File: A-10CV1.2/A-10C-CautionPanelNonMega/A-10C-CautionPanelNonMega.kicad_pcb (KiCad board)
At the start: 2 copper layers, 129.5 x 85.1 mm, 29 parts, among them J1 Barrel_Jack, J10 Conn_01x24, J11 Conn_01x24, J13 Conn_01x03, J2 Nano Pins 1-15, J3 Nano Pins 16-30 (reversed), J4 Serial Tx/Rx, J8 Conn_01x24, J9 Conn_01x24, Q1 BC338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

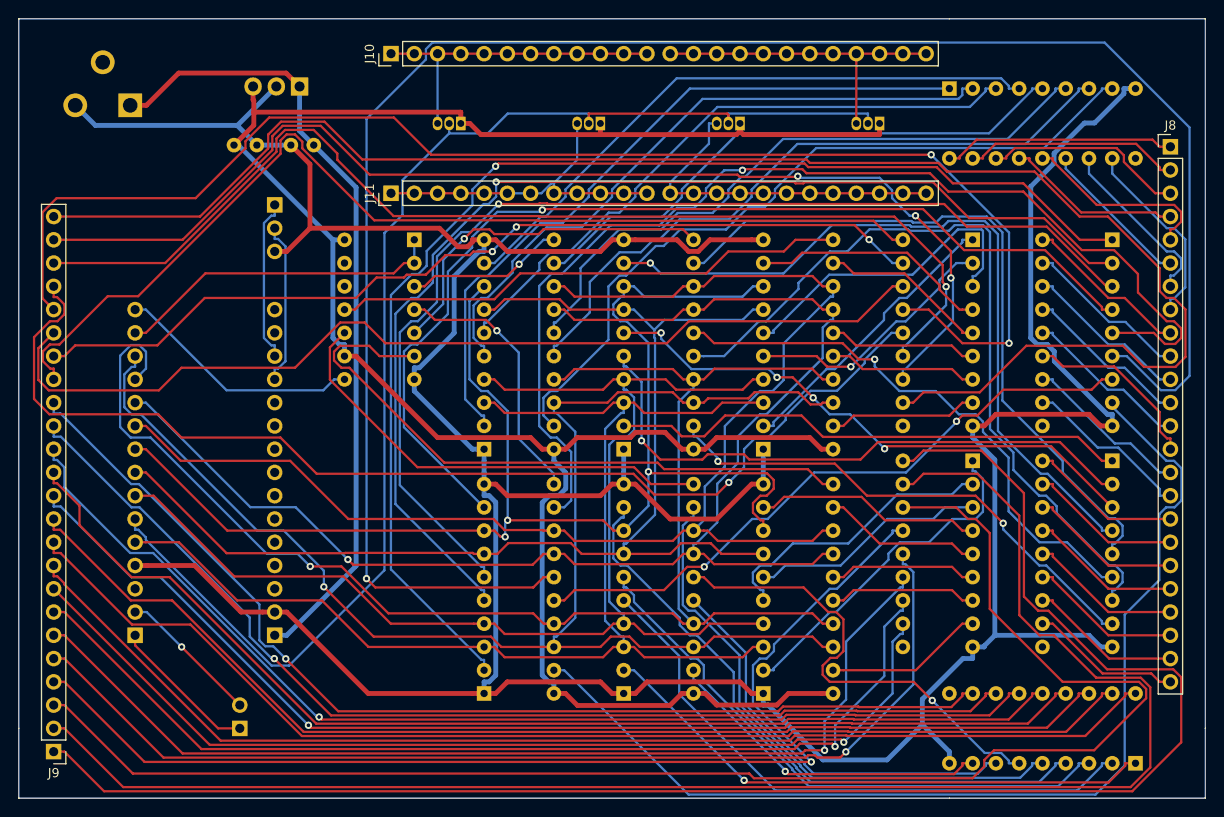
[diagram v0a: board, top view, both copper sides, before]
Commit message: First bits of working code completed. May be changed in favor of single event vs 48 events.
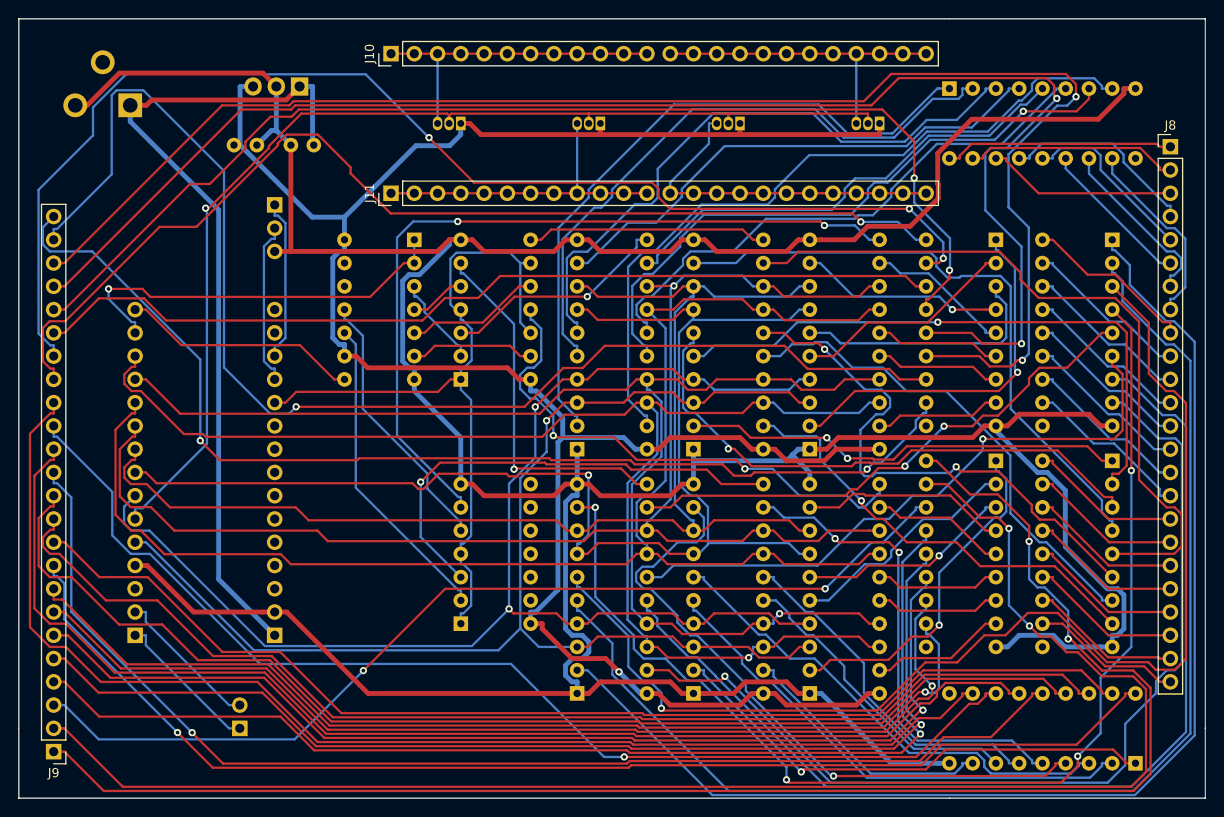
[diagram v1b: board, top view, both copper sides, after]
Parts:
- added U15: 74LS08, Package_DIP:DIP-14_W7.62mm, B.Cu at (97.8, 85.1)
- added U16: 74LS08, Package_DIP:DIP-14_W7.62mm, B.Cu at (97.8, 111.8)
- moved U10 10.2 mm to (110.5, 119.4)
- moved U9 10.2 mm to (110.5, 92.7)
- moved U11 7.62 mm to (123.2, 92.7)
- moved U13 7.62 mm to (123.2, 119.4)
- moved U12 5.08 mm to (135.9, 119.4)
- moved U14 5.08 mm to (135.9, 92.7)
- moved U5 2.54 mm to (156.2, 94.0)
- moved U7 2.54 mm to (156.2, 69.8)
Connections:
- J3 pad 11: Net-(J3-Pad11) -> /CE
- U8 pad 10: /CP4 -> /CPP4
- U8 pad 11: /CP5 -> /CPP5
- U8 pad 3: /CP0 -> /CPP0
- U8 pad 4: /CP1 -> /CPP1
- U8 pad 5: /CP2 -> /CPP2
- U8 pad 6: /CP3 -> /CPP3
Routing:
- net Net-(U10-Pad15): track 207.1 -> 68.0 mm
- net /CE: track 0.00 -> 83.4 mm
- net Net-(U10-Pad12): track 121.1 -> 59.2 mm, vias 1 -> 2
- net /DO3: track 167.3 -> 107.5 mm, vias 0 -> 2
- net /FO8: track 178.7 -> 120.2 mm, vias 0 -> 2
- net /FO6: track 122.7 -> 166.9 mm, vias 1 -> 2
- net Net-(U10-Pad16): track 71.0 -> 114.5 mm, vias 2 -> 0
- net /FO5: track 123.0 -> 164.1 mm, vias 1 -> 2
- net /FO2: track 100.4 -> 136.8 mm
- net /CPP4: track 0.00 -> 34.6 mm
- net Net-(U11-Pad16): track 86.8 -> 54.3 mm
- net /CP5: track 56.5 -> 86.7 mm, vias 0 -> 2
- net /CPP5: track 0.00 -> 29.7 mm
- net GND: track 420.4 -> 448.0 mm
- net /FO4: track 151.8 -> 126.1 mm
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
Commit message: Tweaking timing for Nano to 8 bit interface.
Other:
- board text added: "Rx Tx"
- board text added: "Serial Data (From RS-485)"
- board text removed: "R T"
- board text removed: "Serial Data (RS-485)"
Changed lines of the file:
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@@
     )
   )
-  (gr_text "R\n\nT" (at 76.2 121.92) (layer B.SilkS)
+  (gr_text "Rx\n\nTx" (at 77.47 121.92) (layer B.SilkS)
     (effects (font (size 1 1) (thickness 0.15)) (justify mirror))
   )
-  (gr_text "Serial Data (RS-485)" (at 86.36 120.65) (layer B.SilkS)
+  (gr_text " Serial Data \n(From RS-485)" (at 86.36 121.92) (layer B.SilkS)
     (effects (font (size 1 1) (thickness 0.15)) (justify mirror))
   )

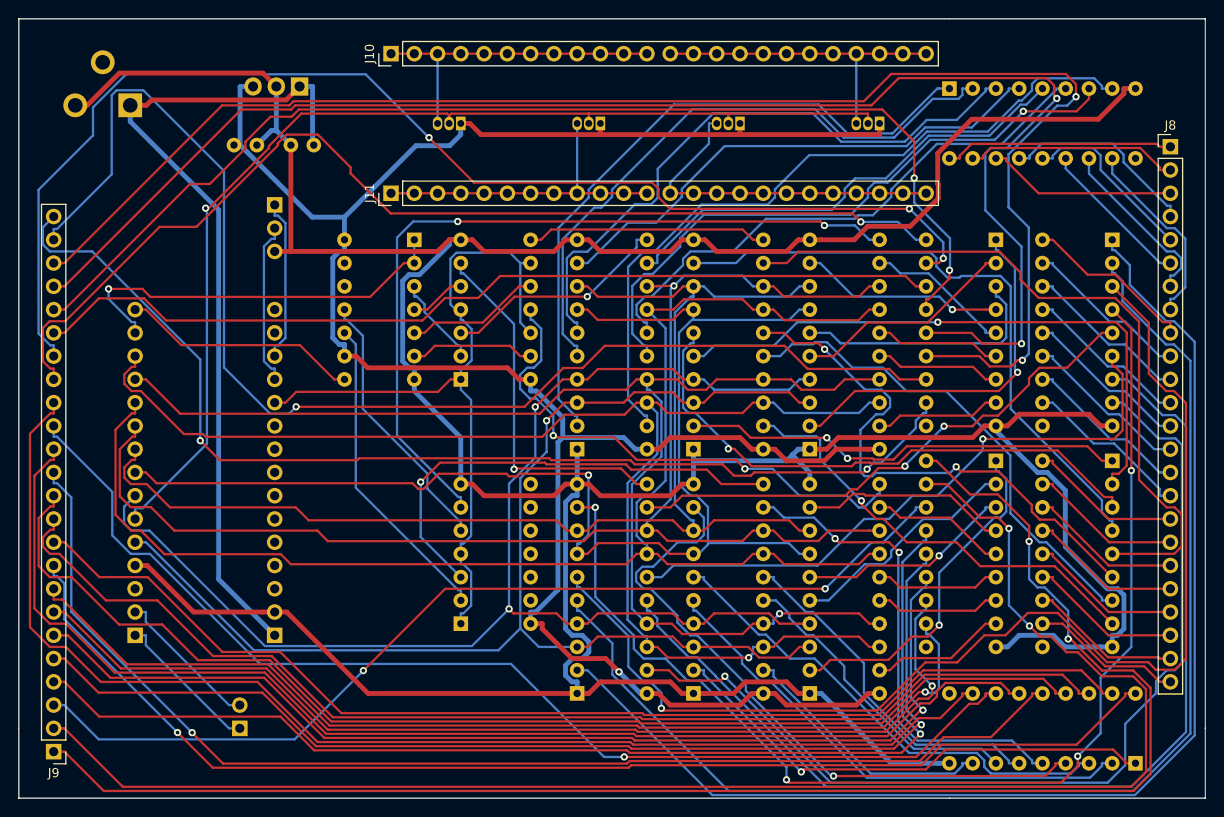
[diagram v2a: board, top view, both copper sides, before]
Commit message: Updating RS port to three pin
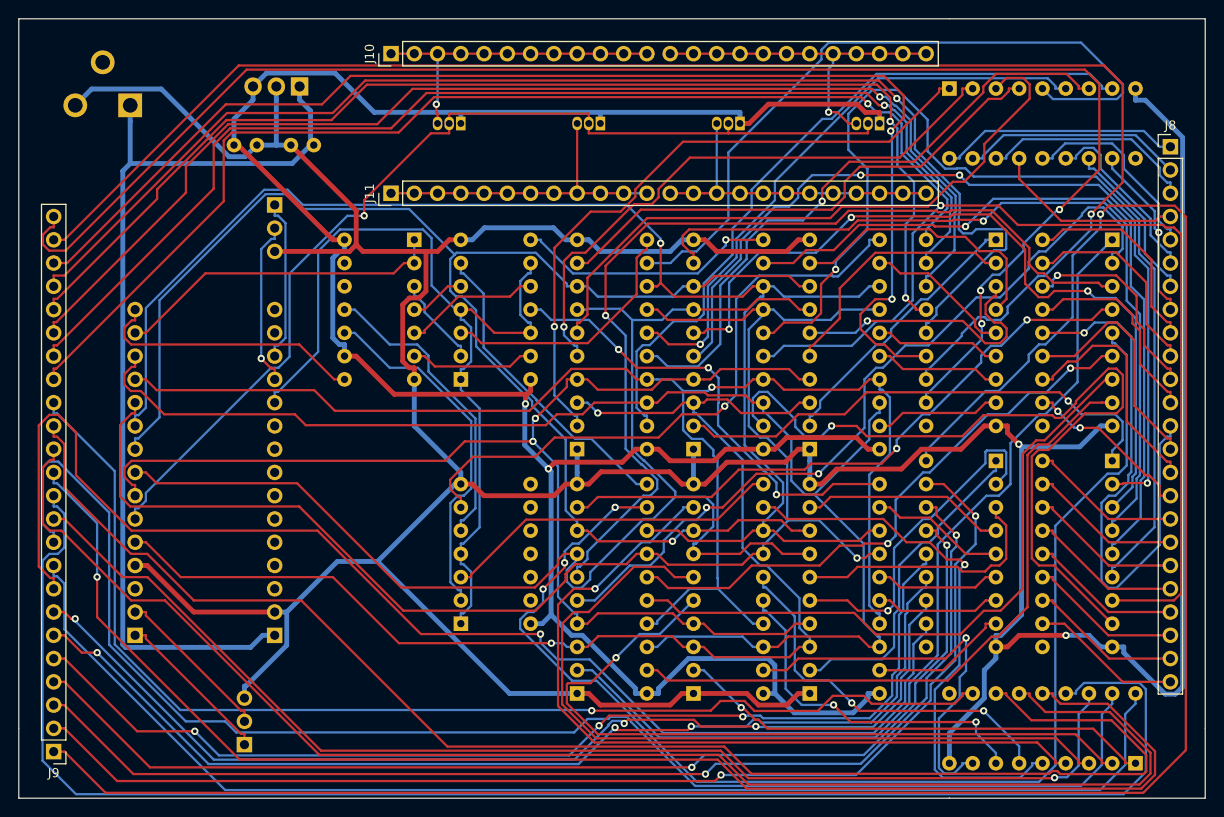
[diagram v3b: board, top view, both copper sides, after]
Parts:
- J4: value Serial Tx/Rx -> Serial Data (via RS-485); footprint Connector_PinHeader_2.54mm:PinHeader_1x02_P2.54mm_Vertical -> Connector_PinHeader_2.54mm:PinHeader_1x03_P2.54mm_Vertical
- U1: value LM7805_TO220 -> L78S05CV_TO220
- moved J4 1.85 mm to (74.2, 125.0)
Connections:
- net Net-(J2-Pad14) renamed /DS
- net Net-(J2-Pad15) renamed /CP
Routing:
- net Net-(U10-Pad12): track 59.2 -> 140.0 mm, vias 2 -> 3
- net /DO1: track 171.7 -> 231.9 mm, vias 2 -> 1
- net Net-(U10-Pad9): track 128.4 -> 68.4 mm, vias 4 -> 2
- net Net-(U11-Pad15): track 60.1 -> 114.5 mm, vias 2 -> 1
- net /FO8: track 120.2 -> 171.6 mm, vias 2 -> 3
- net Net-(U11-Pad16): track 54.3 -> 105.0 mm, vias 0 -> 1
- net Net-(U10-Pad5): track 136.4 -> 87.6 mm, vias 0 -> 2
- net /BO5: track 18.3 -> 61.6 mm, vias 0 -> 1
- net /EO4: track 130.7 -> 172.8 mm
- net Net-(U10-Pad16): track 114.5 -> 72.5 mm
- net Net-(U11-Pad19): track 48.5 -> 89.8 mm
- net /DO2: track 169.8 -> 130.8 mm
- net /EO7: track 124.3 -> 159.9 mm, vias 1 -> 0
- net Net-(U13-Pad6): track 53.3 -> 86.5 mm
- net Net-(U10-Pad19): track 106.1 -> 73.6 mm, vias 1 -> 0
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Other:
- board text added: "GND Rx Tx"
- board text removed: "Rx Tx"

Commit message: Saving before PC reset
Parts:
- moved U1 2.54 mm to (80.2, 50.6)
- moved C1 2.54 mm to (81.7, 57.0)
- moved C2 2.54 mm to (73.0, 57.0)
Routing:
- net /EO3: track 132.5 -> 248.2 mm, vias 1 -> 0
- net /DO1: track 231.9 -> 132.0 mm
- net Net-(U11-Pad15): track 114.5 -> 49.3 mm
- net Net-(U10-Pad12): track 140.0 -> 74.9 mm, vias 3 -> 0
- net Net-(U11-Pad16): track 105.0 -> 56.1 mm, vias 1 -> 3
- net Net-(U11-Pad5): track 96.8 -> 51.6 mm, vias 3 -> 2
- net Net-(U10-Pad9): track 68.4 -> 112.1 mm
- net Net-(U10-Pad16): track 72.5 -> 116.0 mm
- net /BO5: track 61.6 -> 18.3 mm, vias 1 -> 0
- net Net-(U11-Pad19): track 89.8 -> 48.4 mm
- net Net-(U10-Pad6): track 103.1 -> 143.1 mm
- net Net-(U10-Pad15): track 64.1 -> 102.4 mm, vias 2 -> 3
- net /FO8: track 171.6 -> 135.9 mm, vias 3 -> 0
- net /FO7: track 169.0 -> 133.3 mm, vias 1 -> 0
- net Net-(U10-Pad5): track 87.6 -> 119.8 mm, vias 2 -> 1
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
